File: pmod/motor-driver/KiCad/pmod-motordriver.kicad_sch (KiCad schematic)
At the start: 14 parts, among them J1 Conn_01x06_Pin, J2 Screw_Terminal_01x02, J3 Screw_Terminal_01x02, J4 Screw_Terminal_01x02, Q1 AO3401A, U1 DRV8833PWP

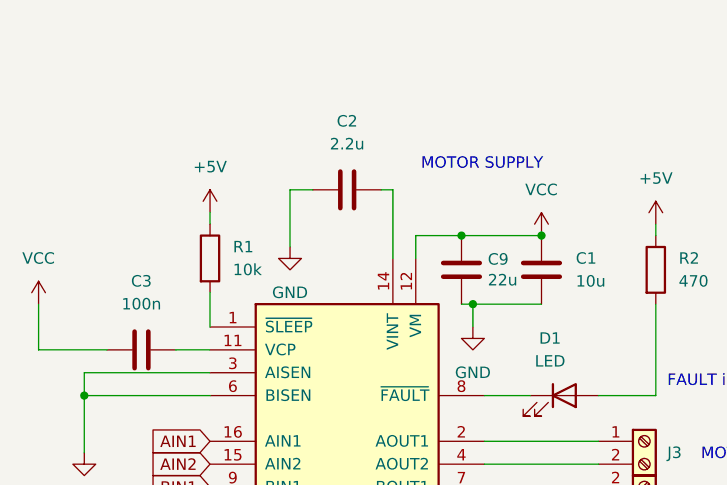
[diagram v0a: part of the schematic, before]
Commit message: fix: prepare all board for manufacturing
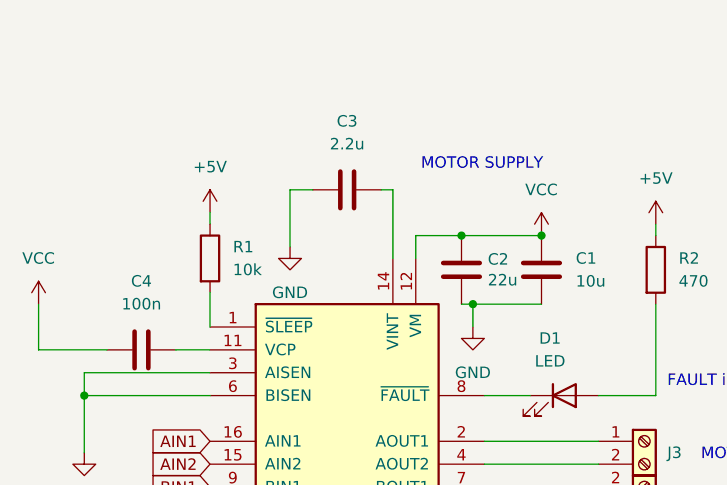
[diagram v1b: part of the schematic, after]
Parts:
- renumbered C9 to C2, C2 to C3, C3 to C4

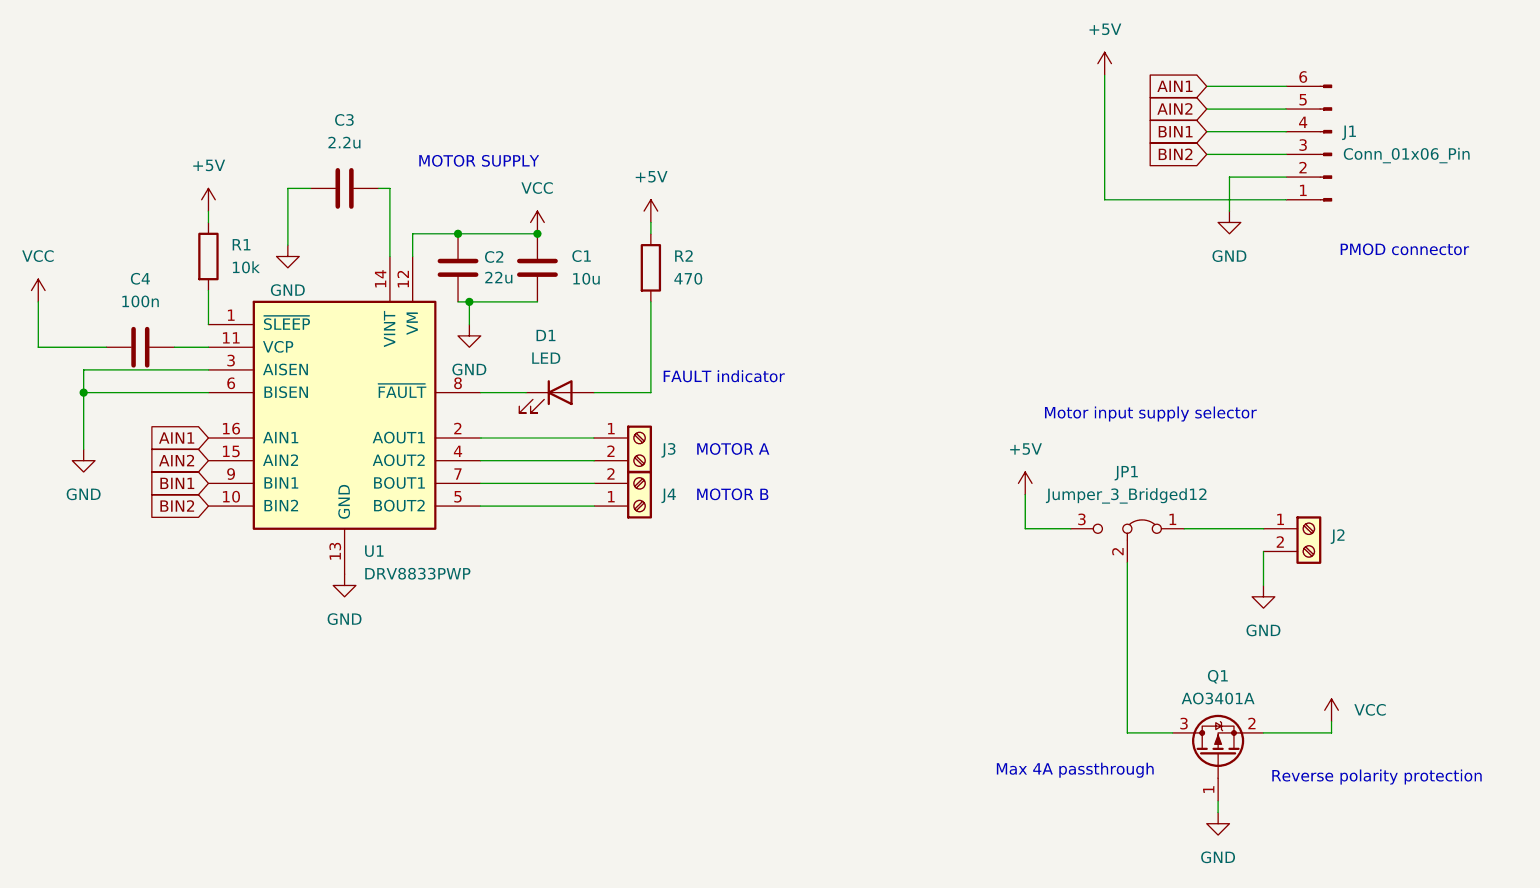
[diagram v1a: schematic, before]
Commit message: docs: add images, fix docs
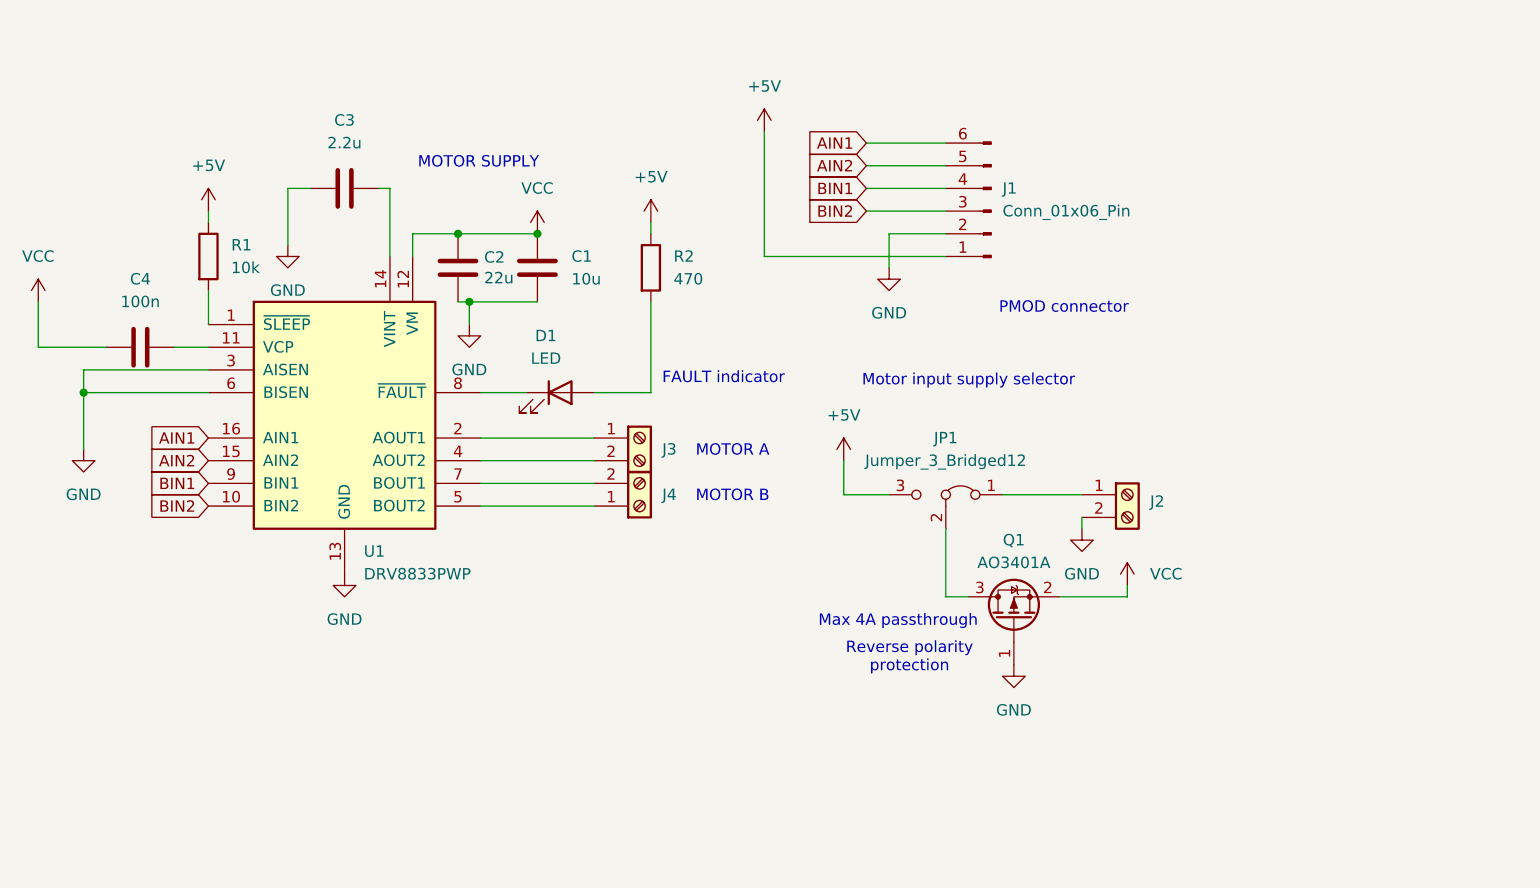
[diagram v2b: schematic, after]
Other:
- moved on the sheet: J1, J2, JP1, Q1

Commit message: fix: motor driver board V2
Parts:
- removed J3, J4: Screw_Terminal_01x02, TerminalBlock_TE-Connectivity:TerminalBlock_TE_282834-2_1x02_P2.54mm_Horizontal, symbol Connector:Screw_Terminal_01x02
- added H1: MountingHole, MountingHole:MountingHole_3.2mm_M3, symbol Mechanical:MountingHole
- added J4: Conn_01x04_Pin, Connector_PinHeader_2.54mm:PinHeader_1x04_P2.54mm_Vertical, symbol Connector:Conn_01x04_Pin
- added J5: Screw_Terminal_01x04, TerminalBlock_Phoenix:TerminalBlock_Phoenix_MKDS-1,5-4-5.08_1x04_P5.08mm_Horizontal, symbol Connector:Screw_Terminal_01x04
- J2: footprint TerminalBlock_TE-Connectivity:TerminalBlock_TE_282834-2_1x02_P2.54mm_Horizontal -> TerminalBlock_Phoenix:TerminalBlock_Phoenix_MKDS-1,5-2-5.08_1x02_P5.08mm_Horizontal
- R2: value 470 -> 1k; LCSC C23179 -> C21190
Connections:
- net BOUT2: now reaches U1.5 (BOUT2)
- net BOUT2: now also J4.3 (Pin_3), J5.3 (Pin_3)
- net BOUT1: now reaches U1.7 (BOUT1)
- net BOUT1: now also J4.4 (Pin_4), J5.4 (Pin_4)
- net AOUT1: now reaches U1.2 (AOUT1)
- net AOUT1: now also J4.1 (Pin_1), J5.1 (Pin_1)
- net AOUT2: now reaches U1.4 (AOUT2)
- net AOUT2: now also J4.2 (Pin_2), J5.2 (Pin_2)
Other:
- note added: "2.54mm pin header for alternative connection"
- note removed: "MOTOR A"
- note removed: "MOTOR B"
